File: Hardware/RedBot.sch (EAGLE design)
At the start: 39 parts, among them U2 TB6612FNG, U3 MIC5219 5V

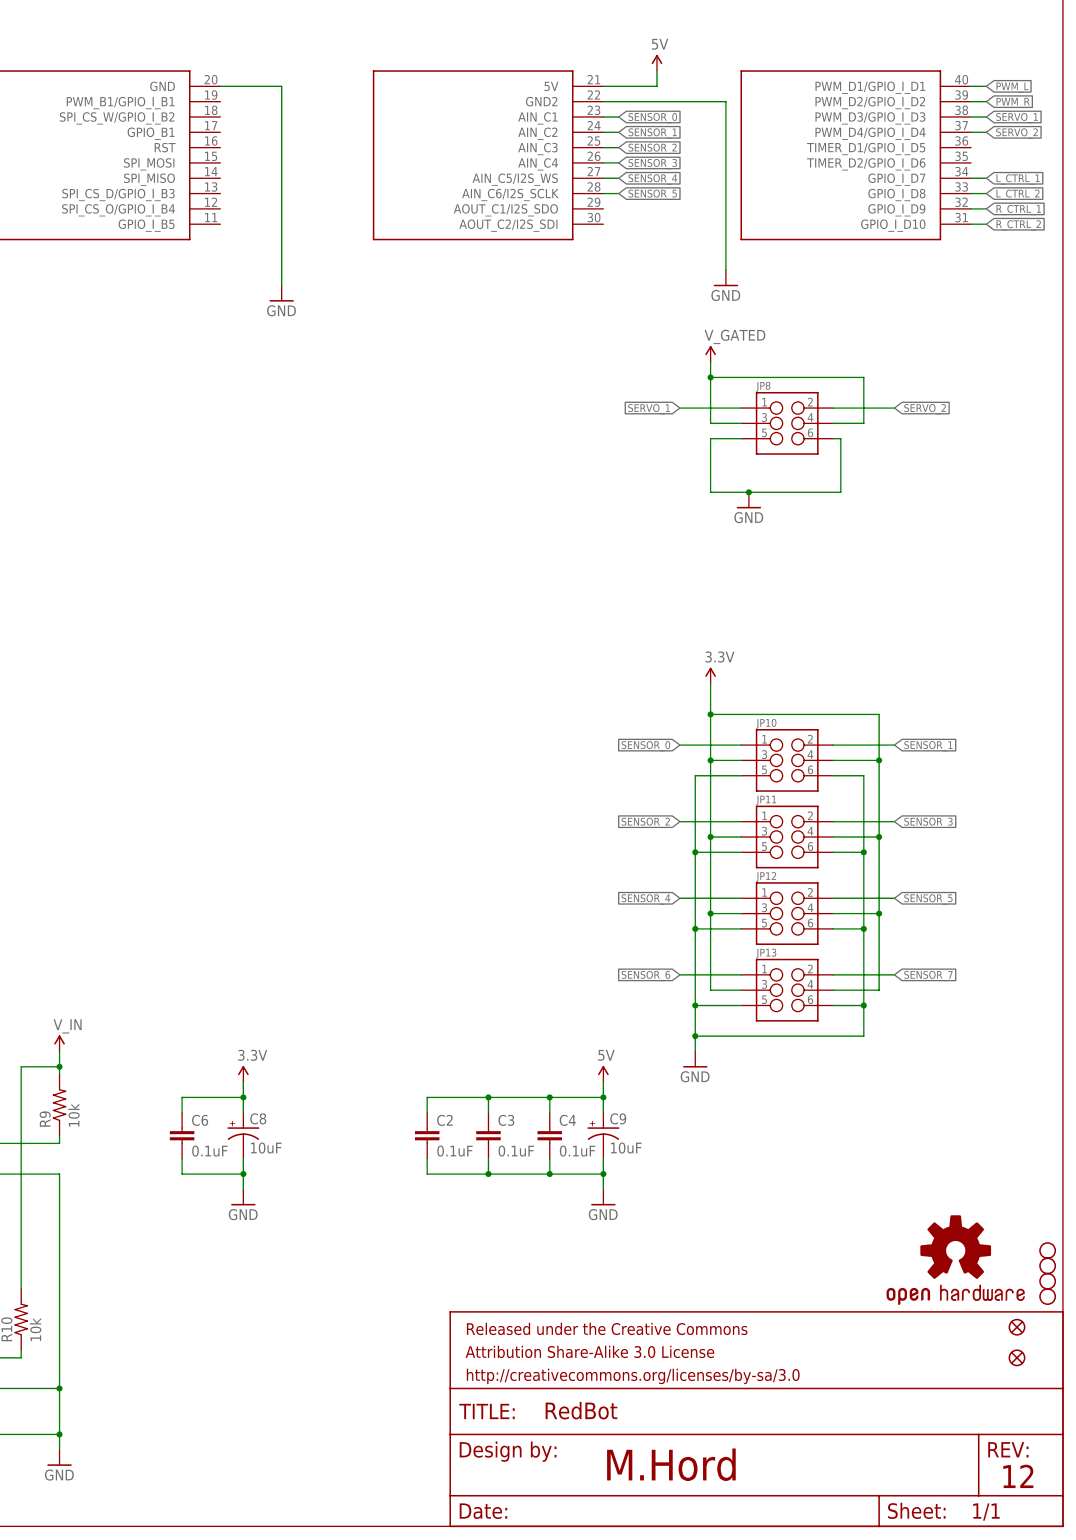
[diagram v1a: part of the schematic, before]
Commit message: Updated parts to use through hole for sensor/servo connectors
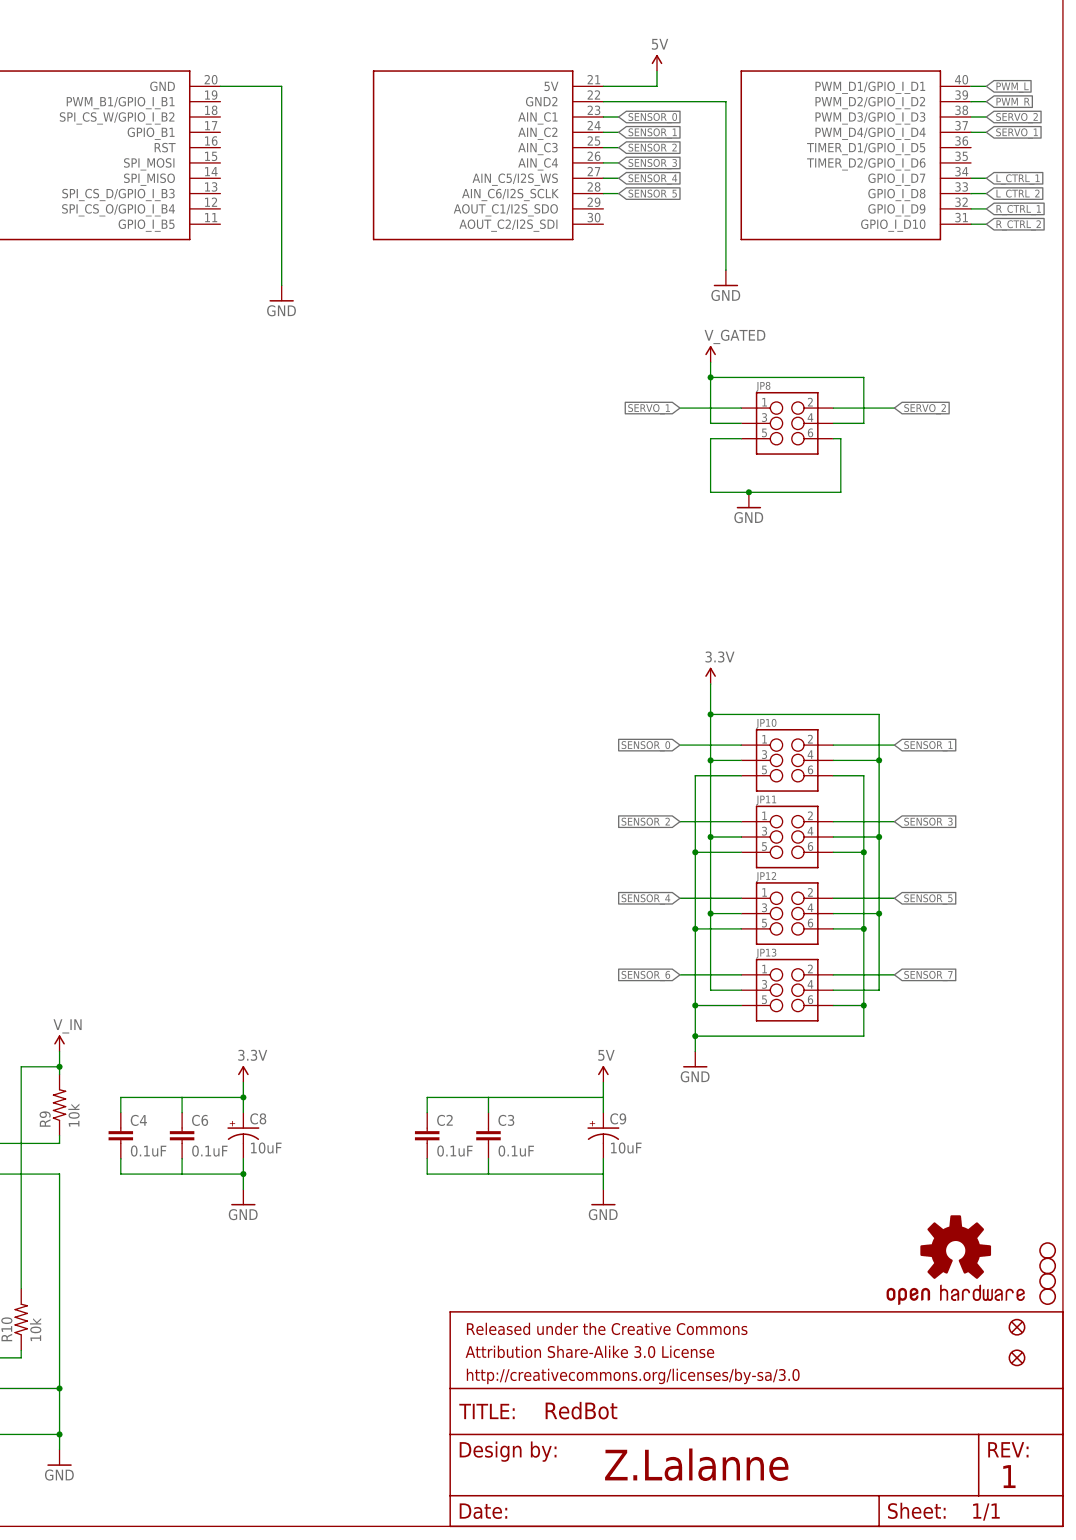
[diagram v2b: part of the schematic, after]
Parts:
- JP10, JP11, JP12, JP13, JP8: device SparkFun-Connectors:M03X2SMT -> SparkFun-Connectors:M03X22X3_SILK_SM
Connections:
- net 3.3V: now also C4.1
- net 5V: no longer C4.1
- net SERVO_1: now also LAUNCHPAD.PWM_D4/GPIO_I_D4; no longer LAUNCHPAD.PWM_D3/GPIO_I_D3
- net SERVO_2: now also LAUNCHPAD.PWM_D3/GPIO_I_D3; no longer LAUNCHPAD.PWM_D4/GPIO_I_D4
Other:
- note added: "1"
- note added: "Z.Lalanne"
- note removed: "12"
- note removed: "M.Hord"
- moved on the sheet: C4
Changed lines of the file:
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@@
 <part name="STANDOFF3" library="SparkFun-Electromechanical" deviceset="STAND-OFF" device=""/>
 <part name="STANDOFF4" library="SparkFun-Electromechanical" deviceset="STAND-OFF" device=""/>
-<part name="JP8" library="SparkFun-Connectors" deviceset="M03X2" device="SMT"/>
-<part name="JP10" library="SparkFun-Connectors" deviceset="M03X2" device="SMT"/>
-<part name="JP11" library="SparkFun-Connectors" deviceset="M03X2" device="SMT"/>
-<part name="JP12" library="SparkFun-Connectors" deviceset="M03X2" device="SMT"/>
-<part name="JP13" library="SparkFun-Connectors" deviceset="M03X2" device="SMT"/>
+<part name="JP8" library="SparkFun-Connectors" deviceset="M03X2" device="2X3_SILK_SM"/>
+<part name="JP10" library="SparkFun-Connectors" deviceset="M03X2" device="2X3_SILK_SM"/>
+<part name="JP11" library="SparkFun-Connectors" deviceset="M03X2" device="2X3_SILK_SM"/>
+<part name="JP12" library="SparkFun-Connectors" deviceset="M03X2" device="2X3_SILK_SM"/>
+<part name="JP13" library="SparkFun-Connectors" deviceset="M03X2" device="2X3_SILK_SM"/>
 <part name="V_GATE" library="SparkFun-Aesthetics" deviceset="V_BATT" device="" value="V_GATED"/>
 <part name="GND10" library="SparkFun-Aesthetics" deviceset="GND" device=""/>
@@
 <wire x1="406.4" y1="254" x2="0" y2="254" width="0.1524" layer="94"/>
 <wire x1="0" y1="254" x2="0" y2="0" width="0.1524" layer="94"/>
-<text x="330.2" y="7.62" size="5.08" layer="94">M.Hord</text>
-<text x="395.986" y="6.35" size="3.81" layer="94">12</text>
+<text x="330.2" y="7.62" size="5.08" layer="94">Z.Lalanne</text>
+<text x="395.986" y="6.35" size="3.81" layer="94">1</text>
 </plain>
 <instances>
@@
 <instance part="U2" gate="G$1" x="63.5" y="129.54"/>
 <instance part="JP3" gate="G$1" x="38.1" y="40.64"/>
-<instance part="C4" gate="G$1" x="321.31" y="63.5"/>
+<instance part="C4" gate="G$1" x="250.19" y="63.5"/>
 <instance part="C6" gate="G$1" x="260.35" y="63.5"/>
 <instance part="S1" gate="G$1" x="224.79" y="22.86"/>
@@
 </segment>
 <segment>
+<pinref part="LAUNCHPAD" gate="G$1" pin="PWM_D4/GPIO_I_D4"/>
+<wire x1="391.16" y1="231.14" x2="393.7" y2="231.14" width="0.1524" layer="91"/>
+<label x="393.7" y="231.14" size="1.27" layer="95" xref="yes"/>
+</segment>
+</net>
+<net name="PWML" class="0">
+<segment>
+<pinref part="U2" gate="G$1" pin="PWMA"/>
+<wire x1="78.74" y1="139.7" x2="88.9" y2="139.7" width="0.1524" layer="91"/>
+<label x="88.9" y="139.7" size="1.27" layer="95" xref="yes"/>
+</segment>
+</net>
+<net name="PWMR" class="0">
+<segment>
+<pinref part="U2" gate="G$1" pin="PWMB"/>
+<wire x1="78.74" y1="119.38" x2="88.9" y2="119.38" width="0.1524" layer="91"/>
+<label x="88.9" y="119.38" size="1.27" layer="95" xref="yes"/>
+</segment>
+</net>
+<net name="SERVO_2" class="0">
+<segment>
+<pinref part="JP8" gate="G$1" pin="2"/>
+<wire x1="368.3" y1="185.42" x2="378.46" y2="185.42" width="0.1524" layer="91"/>
+<label x="378.46" y="185.42" size="1.27" layer="95" xref="yes"/>
+</segment>
+<segment>
 <pinref part="LAUNCHPAD" gate="G$1" pin="PWM_D3/GPIO_I_D3"/>
 <wire x1="391.16" y1="233.68" x2="393.7" y2="233.68" width="0.1524" layer="91"/>
 <label x="393.7" y="233.68" size="1.27" layer="95" xref="yes"/>
-</segment>
-</net>
-<net name="PWML" class="0">
-<segment>
-<pinref part="U2" gate="G$1" pin="PWMA"/>
-<wire x1="78.74" y1="139.7" x2="88.9" y2="139.7" width="0.1524" layer="91"/>
-<label x="88.9" y="139.7" size="1.27" layer="95" xref="yes"/>
-</segment>
-</net>
-<net name="PWMR" class="0">
-<segment>
-<pinref part="U2" gate="G$1" pin="PWMB"/>
-<wire x1="78.74" y1="119.38" x2="88.9" y2="119.38" width="0.1524" layer="91"/>
-<label x="88.9" y="119.38" size="1.27" layer="95" xref="yes"/>
-</segment>
-</net>
-<net name="SERVO_2" class="0">
-<segment>
-<pinref part="JP8" gate="G$1" pin="2"/>
-<wire x1="368.3" y1="185.42" x2="378.46" y2="185.42" width="0.1524" layer="91"/>
-<label x="378.46" y="185.42" size="1.27" layer="95" xref="yes"/>
-</segment>
-<segment>
-<pinref part="LAUNCHPAD" gate="G$1" pin="PWM_D4/GPIO_I_D4"/>
-<wire x1="391.16" y1="231.14" x2="393.7" y2="231.14" width="0.1524" layer="91"/>
-<label x="393.7" y="231.14" size="1.27" layer="95" xref="yes"/>
 </segment>
 </net>
@@
 <wire x1="260.35" y1="58.42" x2="270.51" y2="58.42" width="0.1524" layer="91"/>
 <junction x="270.51" y="58.42"/>
-</segment>
-<segment>
+<pinref part="C4" gate="G$1" pin="2"/>
+<wire x1="250.19" y1="60.96" x2="250.19" y2="58.42" width="0.2032" layer="91"/>
+<wire x1="250.19" y1="58.42" x2="260.35" y2="58.42" width="0.2032" layer="91"/>
+</segment>
+<segment>
+<pinref part="C9" gate="G$1" pin="-"/>
 <pinref part="GND17" gate="1" pin="GND"/>
-<pinref part="C9" gate="G$1" pin="-"/>
 <wire x1="330.2" y1="55.88" x2="330.2" y2="58.42" width="0.1524" layer="91"/>
 <wire x1="330.2" y1="58.42" x2="330.2" y2="60.96" width="0.1524" layer="91"/>
-<junction x="330.2" y="58.42"/>
-<wire x1="330.2" y1="58.42" x2="321.31" y2="58.42" width="0.1524" layer="91"/>
-<wire x1="321.31" y1="58.42" x2="311.15" y2="58.42" width="0.1524" layer="91"/>
 <wire x1="311.15" y1="58.42" x2="300.99" y2="58.42" width="0.1524" layer="91"/>
 <pinref part="C2" gate="G$1" pin="2"/>
@@
 <pinref part="C3" gate="G$1" pin="2"/>
 <wire x1="311.15" y1="60.96" x2="311.15" y2="58.42" width="0.1524" layer="91"/>
-<junction x="311.15" y="58.42"/>
-<pinref part="C4" gate="G$1" pin="2"/>
-<wire x1="321.31" y1="60.96" x2="321.31" y2="58.42" width="0.1524" layer="91"/>
-<junction x="321.31" y="58.42"/>
+<wire x1="311.15" y1="58.42" x2="330.2" y2="58.42" width="0.2032" layer="91"/>
 </segment>
 <segment>
@@
 </segment>
 <segment>
+<pinref part="U$13" gate="G$1" pin="5V"/>
 <pinref part="C9" gate="G$1" pin="+"/>
-<pinref part="U$13" gate="G$1" pin="5V"/>
 <wire x1="330.2" y1="68.58" x2="330.2" y2="71.12" width="0.1524" layer="91"/>
 <wire x1="330.2" y1="71.12" x2="330.2" y2="73.66" width="0.1524" layer="91"/>
-<wire x1="330.2" y1="71.12" x2="321.31" y2="71.12" width="0.1524" layer="91"/>
-<wire x1="321.31" y1="71.12" x2="311.15" y2="71.12" width="0.1524" layer="91"/>
 <wire x1="311.15" y1="71.12" x2="300.99" y2="71.12" width="0.1524" layer="91"/>
-<junction x="330.2" y="71.12"/>
 <pinref part="C2" gate="G$1" pin="1"/>
 <wire x1="300.99" y1="68.58" x2="300.99" y2="71.12" width="0.1524" layer="91"/>
 <pinref part="C3" gate="G$1" pin="1"/>
 <wire x1="311.15" y1="68.58" x2="311.15" y2="71.12" width="0.1524" layer="91"/>
-<junction x="311.15" y="71.12"/>
-<pinref part="C4" gate="G$1" pin="1"/>
-<wire x1="321.31" y1="68.58" x2="321.31" y2="71.12" width="0.1524" layer="91"/>
-<junction x="321.31" y="71.12"/>
+<wire x1="311.15" y1="71.12" x2="330.2" y2="71.12" width="0.2032" layer="91"/>
 </segment>
 <segment>
@@
 <wire x1="260.35" y1="71.12" x2="270.51" y2="71.12" width="0.1524" layer="91"/>
 <junction x="270.51" y="71.12"/>
-</segment>
-<segment>
+<pinref part="C4" gate="G$1" pin="1"/>
+<wire x1="250.19" y1="68.58" x2="250.19" y2="71.12" width="0.2032" layer="91"/>
+<wire x1="250.19" y1="71.12" x2="260.35" y2="71.12" width="0.2032" layer="91"/>
+</segment>
+<segment>
